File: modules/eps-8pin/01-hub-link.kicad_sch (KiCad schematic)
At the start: 6 parts, among them J1 TO-HUB

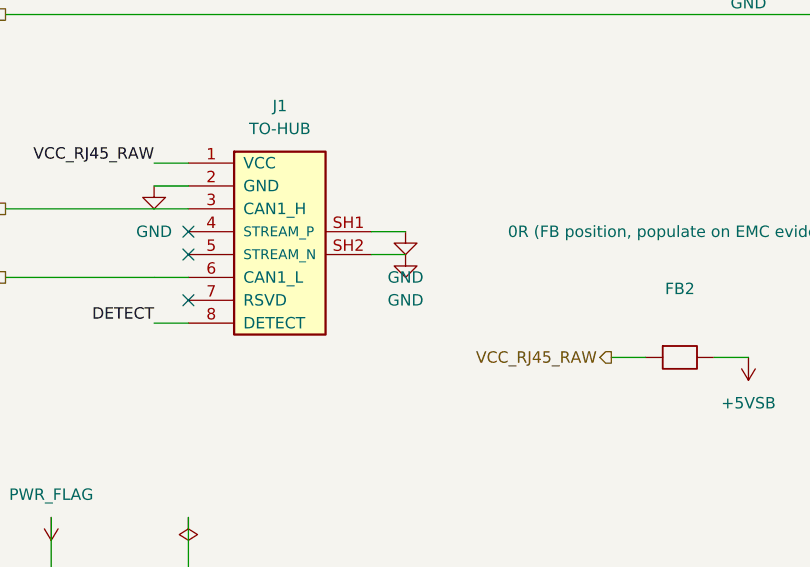
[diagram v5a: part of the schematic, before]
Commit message: Wave-2 EPS finalized: ERC posture + hierarchy-aware audit + driver mutator battery
- name-pin stub ERC: measured KiCad FP class (root local label on {wire,
  sheet-pin} subgraph); root hier labels illegal; erc_exclusions CLASS-LOOSE
  (wrong uuid+position suppressed all 13 - measured) -> driver downgrades
  label_dangling to warning per-board (.kicad_pro, netclasses untouched);
  audit-sch keeps real-dangler teeth (verified). ERC errors 1 vs baseline 2.
- audit-sch.py hierarchy upgrade: per-dir expected instance-path chains
  (root-walked, teeth: bad chain FAILs) + hier/global-label + sheet-pin wire
  anchors -> eps 8/8 ok, ent noise collapsed to its real residuals (FOLLOWUPS).
- driver: project name = .kicad_pro basename (GUI instance-rewrite hazard);
  round-3 mutator battery in-generator (G5 26->7 glyph, identity 58/58 held).
- waivers doc: eps composed-engine floor recorded (1/17/7).

Co-Authored-By: Claude Fable 5 <noreply@anthropic.com>
Claude-Session: https://claude.ai/code/session_01LvfqcnEeuin2oyJQw548EX
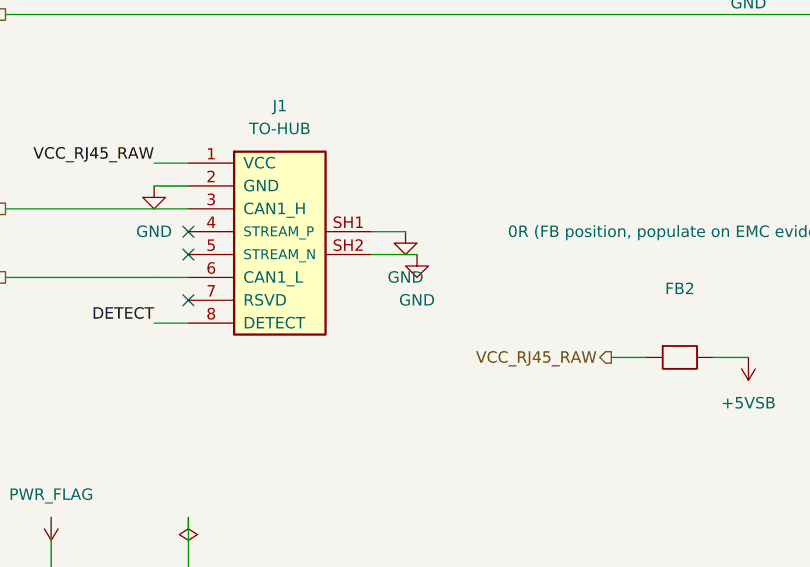
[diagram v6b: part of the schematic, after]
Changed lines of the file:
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@@
 		(pin "SH2")
 		(instances
-			(project "eps-8pin"
+			(project "eps8pin-module"
 				(path "/ef7f6c4c-2dd9-4559-b472-96b33604786a/67f50ca3-8cb0-4aa6-9a3f-011faa4ff8d7" (reference "J1") (unit 1))
 			)
@@
 		(pin "2")
 		(instances
-			(project "eps-8pin"
+			(project "eps8pin-module"
 				(path "/ef7f6c4c-2dd9-4559-b472-96b33604786a/67f50ca3-8cb0-4aa6-9a3f-011faa4ff8d7" (reference "R1") (unit 1))
 			)
@@
 		(pin "2")
 		(instances
-			(project "eps-8pin"
+			(project "eps8pin-module"
 				(path "/ef7f6c4c-2dd9-4559-b472-96b33604786a/67f50ca3-8cb0-4aa6-9a3f-011faa4ff8d7" (reference "C6") (unit 1))
 			)
@@
 		(pin "2")
 		(instances
-			(project "eps-8pin"
+			(project "eps8pin-module"
 				(path "/ef7f6c4c-2dd9-4559-b472-96b33604786a/67f50ca3-8cb0-4aa6-9a3f-011faa4ff8d7" (reference "D1") (unit 1))
 			)
@@
 		(pin "2")
 		(instances
-			(project "eps-8pin"
+			(project "eps8pin-module"
 				(path "/ef7f6c4c-2dd9-4559-b472-96b33604786a/67f50ca3-8cb0-4aa6-9a3f-011faa4ff8d7" (reference "R7") (unit 1))
 			)
@@
 		(pin "2")
 		(instances
-			(project "eps-8pin"
+			(project "eps8pin-module"
 				(path "/ef7f6c4c-2dd9-4559-b472-96b33604786a/67f50ca3-8cb0-4aa6-9a3f-011faa4ff8d7" (reference "FB2") (unit 1))
 			)
@@
 	(wire (pts (xy 143.51 99.06) (xy 147.32 99.06))
 		(stroke (width 0) (type default)))
-	(wire (pts (xy 143.51 101.6) (xy 147.32 101.6))
+	(wire (pts (xy 143.51 101.6) (xy 148.59 101.6))
 		(stroke (width 0) (type default)))
 	(wire (pts (xy 196.85 71.12) (xy 196.85 74.93))
@@
 		(pin "1")
 		(instances
-			(project "eps-8pin"
+			(project "eps8pin-module"
 				(path "/ef7f6c4c-2dd9-4559-b472-96b33604786a/67f50ca3-8cb0-4aa6-9a3f-011faa4ff8d7" (reference "#PWR101") (unit 1))
 			)
@@
 		(pin "1")
 		(instances
-			(project "eps-8pin"
+			(project "eps8pin-module"
 				(path "/ef7f6c4c-2dd9-4559-b472-96b33604786a/67f50ca3-8cb0-4aa6-9a3f-011faa4ff8d7" (reference "#PWR102") (unit 1))
 			)
@@
 		(pin "1")
 		(instances
-			(project "eps-8pin"
+			(project "eps8pin-module"
 				(path "/ef7f6c4c-2dd9-4559-b472-96b33604786a/67f50ca3-8cb0-4aa6-9a3f-011faa4ff8d7" (reference "#PWR103") (unit 1))
 			)
@@
 		(pin "1")
 		(instances
-			(project "eps-8pin"
+			(project "eps8pin-module"
 				(path "/ef7f6c4c-2dd9-4559-b472-96b33604786a/67f50ca3-8cb0-4aa6-9a3f-011faa4ff8d7" (reference "#PWR104") (unit 1))
 			)
@@
 	(symbol
 		(lib_id "cec-power:GND")
-		(at 147.32 101.6 0)
-		(unit 1)
-		(exclude_from_sim no)
-		(in_bom yes)
-		(on_board yes)
-		(dnp no)
-		(property "Reference" "#PWR105" (at 147.32 99.06 0) (effects (font (size 1.27 1.27)) (hide yes)))
-		(property "Value" "GND" (at 147.32 106.68 0) (effects (font (size 1.27 1.27))))
-		(pin "1")
-		(instances
-			(project "eps-8pin"
+		(at 148.59 101.6 0)
+		(unit 1)
+		(exclude_from_sim no)
+		(in_bom yes)
+		(on_board yes)
+		(dnp no)
+		(property "Reference" "#PWR105" (at 148.59 99.06 0) (effects (font (size 1.27 1.27)) (hide yes)))
+		(property "Value" "GND" (at 148.59 106.68 0) (effects (font (size 1.27 1.27))))
+		(pin "1")
+		(instances
+			(project "eps8pin-module"
 				(path "/ef7f6c4c-2dd9-4559-b472-96b33604786a/67f50ca3-8cb0-4aa6-9a3f-011faa4ff8d7" (reference "#PWR105") (unit 1))
 			)
@@
 		(pin "1")
 		(instances
-			(project "eps-8pin"
+			(project "eps8pin-module"
 				(path "/ef7f6c4c-2dd9-4559-b472-96b33604786a/67f50ca3-8cb0-4aa6-9a3f-011faa4ff8d7" (reference "#PWR106") (unit 1))
 			)
@@
 		(pin "1")
 		(instances
-			(project "eps-8pin"
+			(project "eps8pin-module"
 				(path "/ef7f6c4c-2dd9-4559-b472-96b33604786a/67f50ca3-8cb0-4aa6-9a3f-011faa4ff8d7" (reference "#PWR107") (unit 1))
 			)
@@
 		(pin "1")
 		(instances
-			(project "eps-8pin"
+			(project "eps8pin-module"
 				(path "/ef7f6c4c-2dd9-4559-b472-96b33604786a/67f50ca3-8cb0-4aa6-9a3f-011faa4ff8d7" (reference "#PWR108") (unit 1))
 			)
@@
 		(pin "1")
 		(instances
-			(project "eps-8pin"
+			(project "eps8pin-module"
 				(path "/ef7f6c4c-2dd9-4559-b472-96b33604786a/67f50ca3-8cb0-4aa6-9a3f-011faa4ff8d7" (reference "#PWR109") (unit 1))
 			)
@@
 		(pin "1")
 		(instances
-			(project "eps-8pin"
+			(project "eps8pin-module"
 				(path "/ef7f6c4c-2dd9-4559-b472-96b33604786a/67f50ca3-8cb0-4aa6-9a3f-011faa4ff8d7" (reference "#FLG110") (unit 1))
 			)
@@
 		(pin "1")
 		(instances
-			(project "eps-8pin"
+			(project "eps8pin-module"
 				(path "/ef7f6c4c-2dd9-4559-b472-96b33604786a/67f50ca3-8cb0-4aa6-9a3f-011faa4ff8d7" (reference "#FLG111") (unit 1))
 			)
@@
 		(pin "1")
 		(instances
-			(project "eps-8pin"
+			(project "eps8pin-module"
 				(path "/ef7f6c4c-2dd9-4559-b472-96b33604786a/67f50ca3-8cb0-4aa6-9a3f-011faa4ff8d7" (reference "#PWR112") (unit 1))
 			)
